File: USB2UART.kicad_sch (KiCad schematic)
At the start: 12 parts, among them J1 Conn_01x04, J2 Conn_01x03, J3 Conn_01x03, J4 Conn_01x02, J5 Conn_01x02

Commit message: USB2UART
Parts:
- removed J4, J5: Conn_01x02, Connector_JST:JST_GH_SM02B-GHS-TB_1x02-1MP_P1.25mm_Horizontal, symbol Connector_Generic:Conn_01x02
- added J4, J5: Conn_01x03, Connector_JST:JST_GH_SM04B-GHS-TB_1x04-1MP_P1.25mm_Horizontal, symbol Connector_Generic:Conn_01x04
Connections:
- net +5V: now also J4.1 (Pin_1), J5.1 (Pin_1)
- net GND: now also J4.4 (Pin_4), J5.4 (Pin_4)
- new net UART1/RXD: J4.3 (Pin_3)
- new net UART1/TXD: J4.2 (Pin_2)
- new net UART2/RXD: J5.3 (Pin_3)
- new net UART2/TXD: J5.2 (Pin_2)
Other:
- removed sheet STM1_CAN
- removed sheet STM2_CAN
- added sheet UART1 (subsch/UART.kicad_sch)
- added sheet UART2 (subsch/UART.kicad_sch)
- moved on the sheet: J2, J3

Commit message: another right version
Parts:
- J4, J5: value Conn_01x03 -> Conn_01x04
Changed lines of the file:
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@@
     (in_bom yes) (on_board yes)
     (property "Reference" "J5" (id 0) (at 180.594 127 0))
-    (property "Value" "Conn_01x03" (id 1) (at 179.832 123.7866 0)
+    (property "Value" "Conn_01x04" (id 1) (at 179.832 123.7866 0)
       (effects (font (size 1.27 1.27)) (justify left) hide)
     )
@@
     (in_bom yes) (on_board yes)
     (property "Reference" "J4" (id 0) (at 180.594 114.3 0))
-    (property "Value" "Conn_01x03" (id 1) (at 179.832 111.0866 0)
+    (property "Value" "Conn_01x04" (id 1) (at 179.832 111.0866 0)
       (effects (font (size 1.27 1.27)) (justify left) hide)
     )
@@
     )
     (path "/d5c10d34-5ae0-4a6b-bad8-d4ed4b393fc8"
-      (reference "J4") (unit 1) (value "Conn_01x03") (footprint "Connector_JST:JST_GH_SM04B-GHS-TB_1x04-1MP_P1.25mm_Horizontal")
+      (reference "J4") (unit 1) (value "Conn_01x04") (footprint "Connector_JST:JST_GH_SM04B-GHS-TB_1x04-1MP_P1.25mm_Horizontal")
     )
     (path "/5c0ed9d4-4fd9-4462-8972-42835e322755"
-      (reference "J5") (unit 1) (value "Conn_01x03") (footprint "Connector_JST:JST_GH_SM04B-GHS-TB_1x04-1MP_P1.25mm_Horizontal")
+      (reference "J5") (unit 1) (value "Conn_01x04") (footprint "Connector_JST:JST_GH_SM04B-GHS-TB_1x04-1MP_P1.25mm_Horizontal")
     )
     (path "/71b07c00-0314-4dfd-92cb-aca2c9812e1b/e5588e62-caec-4581-8753-afa8055836e7"

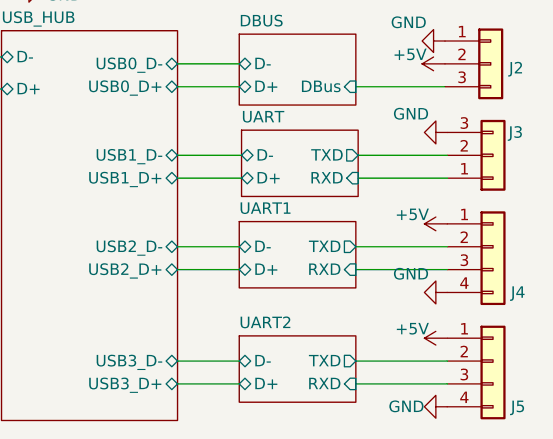
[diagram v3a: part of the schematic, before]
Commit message: Change USB2XXX to USB2UART
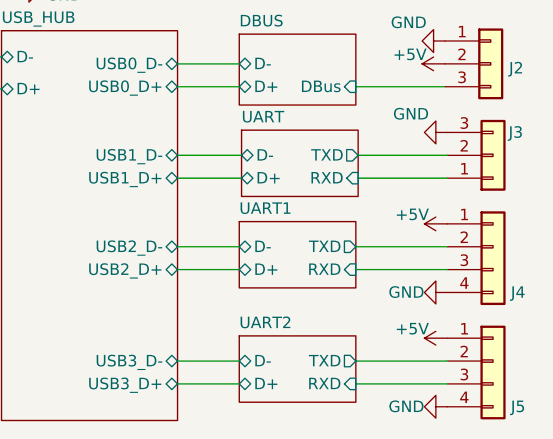
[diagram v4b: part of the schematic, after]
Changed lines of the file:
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@@
       (effects (font (size 1.27 1.27)) hide)
     )
-    (property "Value" "GND" (id 1) (at 170.688 112.268 90)
+    (property "Value" "GND" (id 1) (at 170.18 114.3 90)
       (effects (font (size 1.27 1.27)) (justify right))
     )
